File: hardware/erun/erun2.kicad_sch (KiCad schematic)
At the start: 34 parts, among them J1 Conn_Coaxial, J10 Conn_01x03_Female, J2 HEIDENHAIN_MT25_TTL, J3 TRIGGER_TTL, J4 Conn_01x02_Female, J5 Conn_01x02_Female, J6 Conn_01x02_Female, J7 Conn_01x02_Female, J8 Conn_01x02_Female, J9 Conn_01x03_Female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

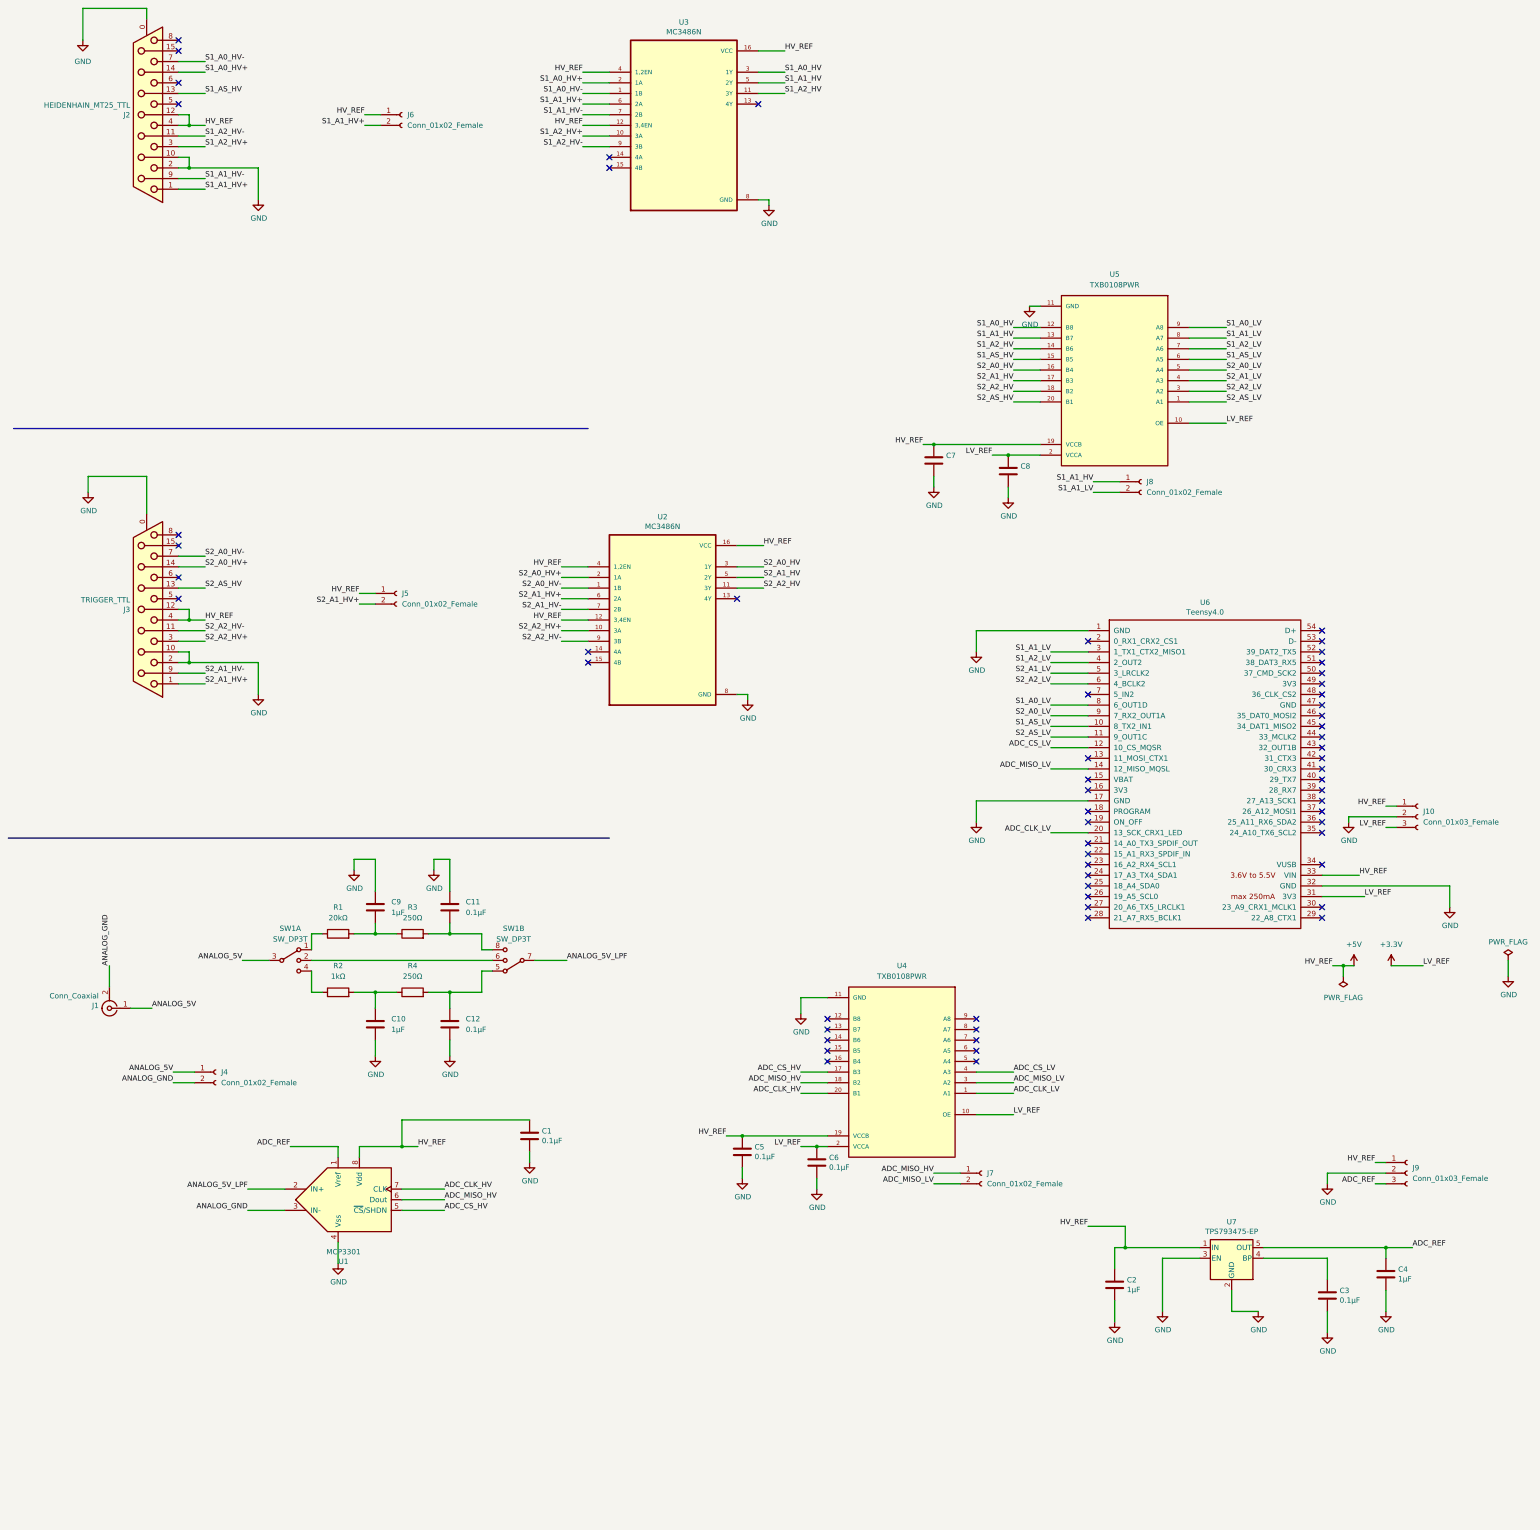
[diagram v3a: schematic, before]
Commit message: PCB 2.1, fixed ADC and moved analog input
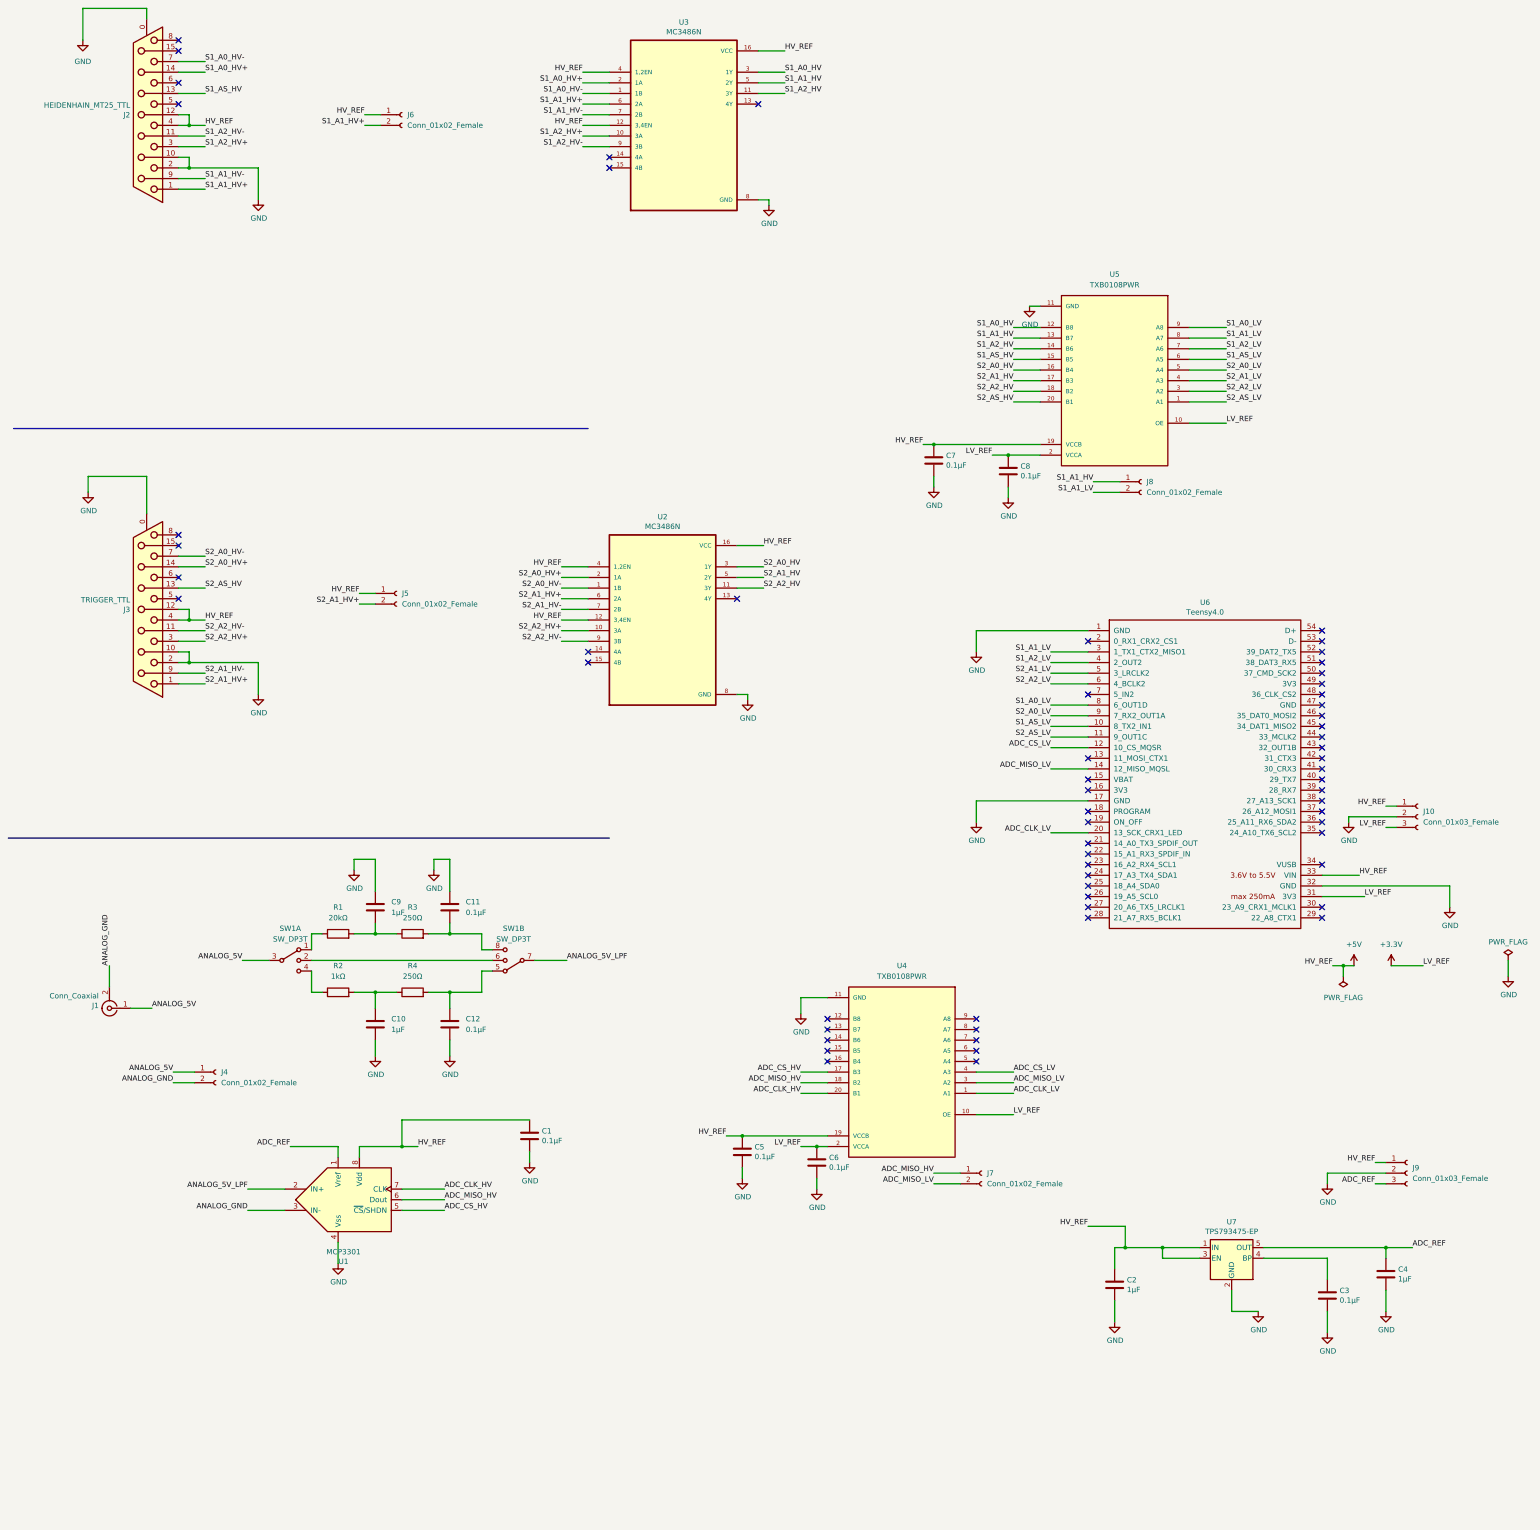
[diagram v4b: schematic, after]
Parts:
- C7, C8: value (none) -> 0.1μF
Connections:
- net +5V: now also U7.3 (EN)
- net GND: no longer U7.3 (EN)
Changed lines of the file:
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@@
   (junction (at 205.74 306.07) (diameter 0) (color 0 0 0 0)
+  )
+  (junction (at 288.29 330.2) (diameter 0) (color 0 0 0 0)
   )
   (junction (at 187.96 303.53) (diameter 0) (color 0 0 0 0)
@@
     (stroke (width 0) (type default) (color 0 0 0 0))
   )
+  (wire (pts (xy 288.29 330.2) (xy 279.4 330.2))
+    (stroke (width 0) (type default) (color 0 0 0 0))
+  )
   (wire (pts (xy 331.47 262.89) (xy 334.01 262.89))
     (stroke (width 0) (type default) (color 0 0 0 0))
@@
     (stroke (width 0) (type default) (color 0 0 0 0))
   )
-  (wire (pts (xy 297.18 330.2) (xy 279.4 330.2))
+  (wire (pts (xy 297.18 330.2) (xy 288.29 330.2))
     (stroke (width 0) (type default) (color 0 0 0 0))
   )
@@
     (stroke (width 0) (type default) (color 0 0 0 0))
   )
+  (wire (pts (xy 288.29 330.2) (xy 288.29 332.74))
+    (stroke (width 0) (type default) (color 0 0 0 0))
+  )
   (wire (pts (xy 270.51 200.66) (xy 261.62 200.66))
-    (stroke (width 0) (type default) (color 0 0 0 0))
-  )
-  (wire (pts (xy 288.29 332.74) (xy 288.29 345.44))
     (stroke (width 0) (type default) (color 0 0 0 0))
   )
@@
     (pin "2")
   )
-  (symbol (lib_id "power:GND") (at 288.29 345.44 0) (unit 1)
-    (in_bom yes) (on_board yes)
-    (property "Reference" "#PWR014" (id 0) (at 288.29 351.79 0)
-      (effects (font (size 1.27 1.27)) hide)
-    )
-    (property "Value" "GND" (id 1) (at 288.417 349.8342 0))
-    (property "Footprint" "" (id 2) (at 288.29 345.44 0)
-      (effects (font (size 1.27 1.27)) hide)
-    )
-    (property "Datasheet" "" (id 3) (at 288.29 345.44 0)
-      (effects (font (size 1.27 1.27)) hide)
-    )
-    (pin "1")
-  )
   (symbol (lib_id "Device:C") (at 137.16 303.53 0) (unit 1)
     (in_bom yes) (on_board yes)
@@
       (effects (font (size 1.27 1.27)) (justify left))
     )
-    (property "Value" "" (id 1) (at 236.601 143.383 0)
+    (property "Value" "0.1μF" (id 1) (at 236.601 143.383 0)
       (effects (font (size 1.27 1.27)) (justify left))
     )
@@
       (effects (font (size 1.27 1.27)) hide)
     )
-    (pin "1")
-    (pin "2")
-    (pin "3")
-    (pin "4")
     (pin "5")
     (pin "6")
@@
     (pin "3")
     (pin "4")
-    (pin "5")
-    (pin "6")
-    (pin "7")
-    (pin "8")
   )
   (symbol (lib_id "Device:R") (at 109.22 269.24 90) (unit 1)
@@
       (effects (font (size 1.27 1.27)) (justify left))
     )
-    (property "Value" "" (id 1) (at 254.381 145.923 0)
+    (property "Value" "0.1μF" (id 1) (at 254.381 145.923 0)
       (effects (font (size 1.27 1.27)) (justify left))
     )
@@
       (reference "#PWR013") (unit 1) (value "GND") (footprint "")
     )
-    (path "/00000000-0000-0000-0000-000061ddc1c0"
-      (reference "#PWR014") (unit 1) (value "GND") (footprint "")
-    )
     (path "/00000000-0000-0000-0000-0000619a1d4f"

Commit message: Added voltage divider
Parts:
- added R5: 9,1kΩ, Resistor_SMD:R_0603_1608Metric, symbol Device:R
- added R6: 2,4kΩ, Resistor_SMD:R_0603_1608Metric, symbol Device:R
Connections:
- net ANALOG_5V: now also R5.2, R6.1; no longer J1.1 (In)
- net ANALOG_GND: now also R6.2
- new net ANALOG_24V: J1.1 (In), R5.1
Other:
- moved on the sheet: C1, J4, U1

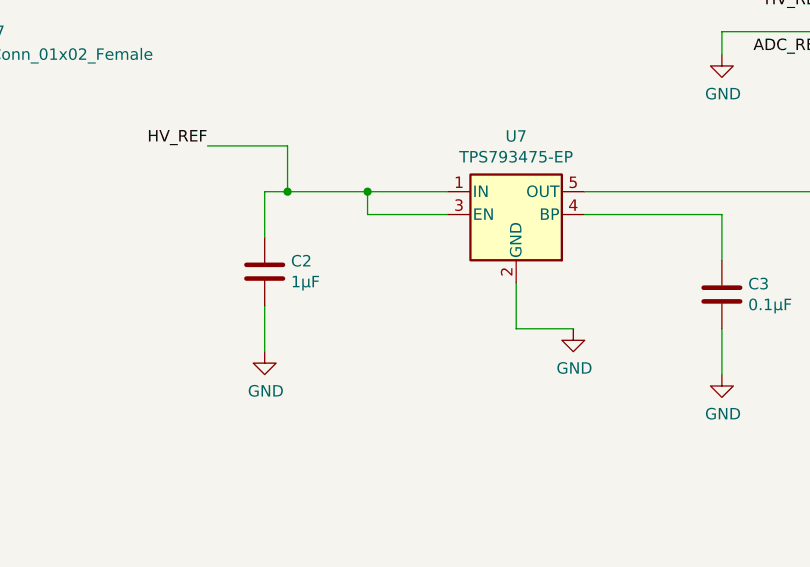
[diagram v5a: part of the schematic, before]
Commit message: First version of PCB board v3.0
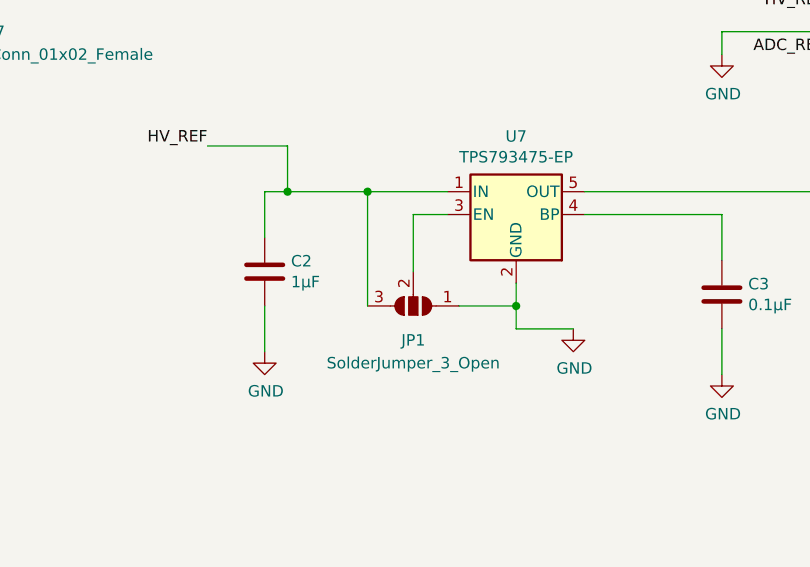
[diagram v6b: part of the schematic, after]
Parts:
- added JP1: SolderJumper_3_Open, Jumper:SolderJumper-3_P1.3mm_Open_Pad1.0x1.5mm_NumberLabels, symbol Jumper:SolderJumper_3_Open
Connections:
- net +5V: now also JP1.3 (B); no longer U7.3 (EN)
- net GND: now also JP1.1 (A)
- new net: JP1.2 (C), U7.3 (EN)
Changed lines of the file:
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@@
   (junction (at 205.74 306.07) (diameter 0) (color 0 0 0 0)
   )
+  (junction (at 304.8 342.9) (diameter 0) (color 0 0 0 0)
+  )
+  (junction (at 187.96 303.53) (diameter 0) (color 0 0 0 0)
+  )
+  (junction (at 93.98 361.95) (diameter 0) (color 0 0 0 0)
+  )
+  (junction (at 100.33 255.27) (diameter 0) (color 0 0 0 0)
+  )
+  (junction (at 55.88 180.34) (diameter 0) (color 0 0 0 0)
+  )
+  (junction (at 55.88 72.39) (diameter 0) (color 0 0 0 0)
+  )
+  (junction (at 331.47 262.89) (diameter 0) (color 0 0 0 0)
+  )
+  (junction (at 118.11 269.24) (diameter 0) (color 0 0 0 0)
+  )
+  (junction (at 251.46 140.97) (diameter 0) (color 0 0 0 0)
+  )
+  (junction (at 279.4 330.2) (diameter 0) (color 0 0 0 0)
+  )
+  (junction (at 64.77 316.23) (diameter 0) (color 0 0 0 0)
+  )
+  (junction (at 55.88 190.5) (diameter 0) (color 0 0 0 0)
+  )
+  (junction (at 233.68 138.43) (diameter 0) (color 0 0 0 0)
+  )
+  (junction (at 341.63 330.2) (diameter 0) (color 0 0 0 0)
+  )
+  (junction (at 55.88 62.23) (diameter 0) (color 0 0 0 0)
+  )
   (junction (at 288.29 330.2) (diameter 0) (color 0 0 0 0)
-  )
-  (junction (at 187.96 303.53) (diameter 0) (color 0 0 0 0)
-  )
-  (junction (at 93.98 361.95) (diameter 0) (color 0 0 0 0)
-  )
-  (junction (at 100.33 255.27) (diameter 0) (color 0 0 0 0)
-  )
-  (junction (at 55.88 180.34) (diameter 0) (color 0 0 0 0)
-  )
-  (junction (at 55.88 72.39) (diameter 0) (color 0 0 0 0)
-  )
-  (junction (at 331.47 262.89) (diameter 0) (color 0 0 0 0)
-  )
-  (junction (at 118.11 269.24) (diameter 0) (color 0 0 0 0)
-  )
-  (junction (at 251.46 140.97) (diameter 0) (color 0 0 0 0)
-  )
-  (junction (at 279.4 330.2) (diameter 0) (color 0 0 0 0)
-  )
-  (junction (at 64.77 316.23) (diameter 0) (color 0 0 0 0)
-  )
-  (junction (at 55.88 190.5) (diameter 0) (color 0 0 0 0)
-  )
-  (junction (at 233.68 138.43) (diameter 0) (color 0 0 0 0)
-  )
-  (junction (at 341.63 330.2) (diameter 0) (color 0 0 0 0)
-  )
-  (junction (at 55.88 62.23) (diameter 0) (color 0 0 0 0)
   )
   (junction (at 100.33 269.24) (diameter 0) (color 0 0 0 0)
@@
     (stroke (width 0) (type default) (color 0 0 0 0))
   )
-  (wire (pts (xy 288.29 330.2) (xy 279.4 330.2))
-    (stroke (width 0) (type default) (color 0 0 0 0))
-  )
   (wire (pts (xy 331.47 262.89) (xy 334.01 262.89))
     (stroke (width 0) (type default) (color 0 0 0 0))
@@
     (stroke (width 0) (type default) (color 0 0 0 0))
   )
-  (wire (pts (xy 297.18 330.2) (xy 288.29 330.2))
+  (wire (pts (xy 279.4 330.2) (xy 288.29 330.2))
     (stroke (width 0) (type default) (color 0 0 0 0))
   )
@@
     (stroke (width 0) (type default) (color 0 0 0 0))
   )
+  (wire (pts (xy 288.29 330.2) (xy 297.18 330.2))
+    (stroke (width 0) (type default) (color 0 0 0 0))
+  )
   (wire (pts (xy 45.72 146.05) (xy 31.75 146.05))
     (stroke (width 0) (type default) (color 0 0 0 0))
@@
     (stroke (width 0) (type default) (color 0 0 0 0))
   )
+  (wire (pts (xy 297.18 332.74) (xy 293.37 332.74))
+    (stroke (width 0) (type default) (color 0 0 0 0))
+  )
   (wire (pts (xy 85.09 269.24) (xy 87.63 269.24))
     (stroke (width 0) (type default) (color 0 0 0 0))
@@
     (stroke (width 0) (type default) (color 0 0 0 0))
   )
+  (wire (pts (xy 288.29 330.2) (xy 288.29 342.9))
+    (stroke (width 0) (type default) (color 0 0 0 0))
+  )
   (wire (pts (xy 252.73 123.19) (xy 259.08 123.19))
     (stroke (width 0) (type default) (color 0 0 0 0))
@@
     (stroke (width 0) (type default) (color 0 0 0 0))
   )
-  (wire (pts (xy 288.29 330.2) (xy 288.29 332.74))
-    (stroke (width 0) (type default) (color 0 0 0 0))
-  )
   (wire (pts (xy 270.51 200.66) (xy 261.62 200.66))
     (stroke (width 0) (type default) (color 0 0 0 0))
@@
     (stroke (width 0) (type default) (color 0 0 0 0))
   )
+  (wire (pts (xy 293.37 332.74) (xy 293.37 339.09))
+    (stroke (width 0) (type default) (color 0 0 0 0))
+  )
   (wire (pts (xy 186.69 172.72) (xy 193.04 172.72))
     (stroke (width 0) (type default) (color 0 0 0 0))
@@
     (stroke (width 0) (type default) (color 0 0 0 0))
   )
-  (wire (pts (xy 297.18 332.74) (xy 288.29 332.74))
-    (stroke (width 0) (type default) (color 0 0 0 0))
-  )
   (wire (pts (xy 252.73 118.11) (xy 259.08 118.11))
     (stroke (width 0) (type default) (color 0 0 0 0))
@@
     (stroke (width 0) (type default) (color 0 0 0 0))
   )
+  (wire (pts (xy 304.8 342.9) (xy 304.8 345.44))
+    (stroke (width 0) (type default) (color 0 0 0 0))
+  )
   (wire (pts (xy 276.86 330.2) (xy 276.86 335.28))
     (stroke (width 0) (type default) (color 0 0 0 0))
@@
     (stroke (width 0) (type default) (color 0 0 0 0))
   )
-  (wire (pts (xy 304.8 340.36) (xy 304.8 345.44))
+  (wire (pts (xy 304.8 340.36) (xy 304.8 342.9))
     (stroke (width 0) (type default) (color 0 0 0 0))
   )
@@
   )
   (wire (pts (xy 201.93 293.37) (xy 208.28 293.37))
+    (stroke (width 0) (type default) (color 0 0 0 0))
+  )
+  (wire (pts (xy 298.45 342.9) (xy 304.8 342.9))
     (stroke (width 0) (type default) (color 0 0 0 0))
   )
@@
     (pin "2")
   )
+  (symbol (lib_id "Jumper:SolderJumper_3_Open") (at 293.37 342.9 180) (unit 1)
+    (in_bom yes) (on_board yes) (fields_autoplaced)
+    (property "Reference" "JP1" (id 0) (at 293.37 346.71 0))
+    (property "Value" "SolderJumper_3_Open" (id 1) (at 293.37 349.25 0))
+    (property "Footprint" "Jumper:SolderJumper-3_P1.3mm_Open_Pad1.0x1.5mm_NumberLabels" (id 2) (at 293.37 342.9 0)
+      (effects (font (size 1.27 1.27)) hide)
+    )
+    (property "Datasheet" "~" (id 3) (at 293.37 342.9 0)
+      (effects (font (size 1.27 1.27)) hide)
+    )
+    (pin "1")
+    (pin "2")
+    (pin "3")
+  )
   (symbol (lib_id "Device:R") (at 91.44 269.24 90) (unit 1)
     (in_bom yes) (on_board yes) (fields_autoplaced)
@@
       (reference "J10") (unit 1) (value "Conn_01x03_Female") (footprint "Connector_PinHeader_2.54mm:PinHeader_1x03_P2.54mm_Vertical")
     )
+    (path "/e2604dce-7bfb-49b0-bb1a-fed36fdb1031"
+      (reference "JP1") (unit 1) (value "SolderJumper_3_Open") (footprint "Jumper:SolderJumper-3_P1.3mm_Open_Pad1.0x1.5mm_NumberLabels")
+    )
     (path "/70a09bf0-5e27-4706-81bb-98a5cf06fcc9"

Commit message: Fixed trace overlapping with hole and changed MCP3301 package from MSOP to SOIC
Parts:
- U1: footprint Package_SO:MSOP-8_3x3mm_P0.65mm -> Package_SO:SOIC-8_3.9x4.9mm_P1.27mm
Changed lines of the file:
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@@
     (property "Reference" "U1" (id 0) (at 80.01 389.4074 0))
     (property "Value" "MCP3301" (id 1) (at 80.01 387.096 0))
-    (property "Footprint" "Package_SO:MSOP-8_3x3mm_P0.65mm" (id 2) (at 101.6 377.19 0)
+    (property "Footprint" "Package_SO:SOIC-8_3.9x4.9mm_P1.27mm" (id 2) (at 101.6 377.19 0)
       (effects (font (size 1.27 1.27)) hide)
     )
@@
       (effects (font (size 1.27 1.27)) hide)
     )
+    (pin "1")
+    (pin "2")
+    (pin "3")
+    (pin "4")
     (pin "5")
     (pin "6")
@@
     (pin "3")
     (pin "4")
+    (pin "5")
+    (pin "6")
+    (pin "7")
+    (pin "8")
   )
   (symbol (lib_id "Device:R") (at 109.22 269.24 90) (unit 1)
@@
     )
     (path "/00000000-0000-0000-0000-000061966194"
-      (reference "U1") (unit 1) (value "MCP3301") (footprint "Package_SO:MSOP-8_3x3mm_P0.65mm")
+      (reference "U1") (unit 1) (value "MCP3301") (footprint "Package_SO:SOIC-8_3.9x4.9mm_P1.27mm")
     )
     (path "/00000000-0000-0000-0000-000061bff331"
